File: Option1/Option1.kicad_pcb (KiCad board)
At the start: 2 copper layers, 86 x 62 mm, 122 parts, among them J1 Conn_02x07_Odd_Even, J1301 Conn_01x02_Socket, J1501 GH-13AB, J1801 Conn_01x08_Socket, J401 Conn_01x05_Pin, J402 Conn_01x04_Pin, J403 Conn_01x05_Pin, J503 KF2EDGKRG-3.5-2*7P, J701 Conn_01x02_Socket, Q1001 JY2302, Q1101 JY2302, Q1401 BC817-40, Q1402 BC817-40, Q601 JY2302, Q901 JY2302, SW401 4*4*1.7, U1401 CH340X, U1601 W25Q512JVEIQ, U1701 TJA1051T-3, U1_I/O_Old1 1989780, U201 U7812-500, U202 K7805-500R2_C909663, U203 SY8089AAAC, U204 SY8089AAAC, U2_CAN1 1989780, U301 TJA1051T-3, U302 MCP2515-I/ST, U801 ESP32-WROOM-32E-N4, U802 MCP23017_SO, X301 XL1EL89CSI-111YLC-8M

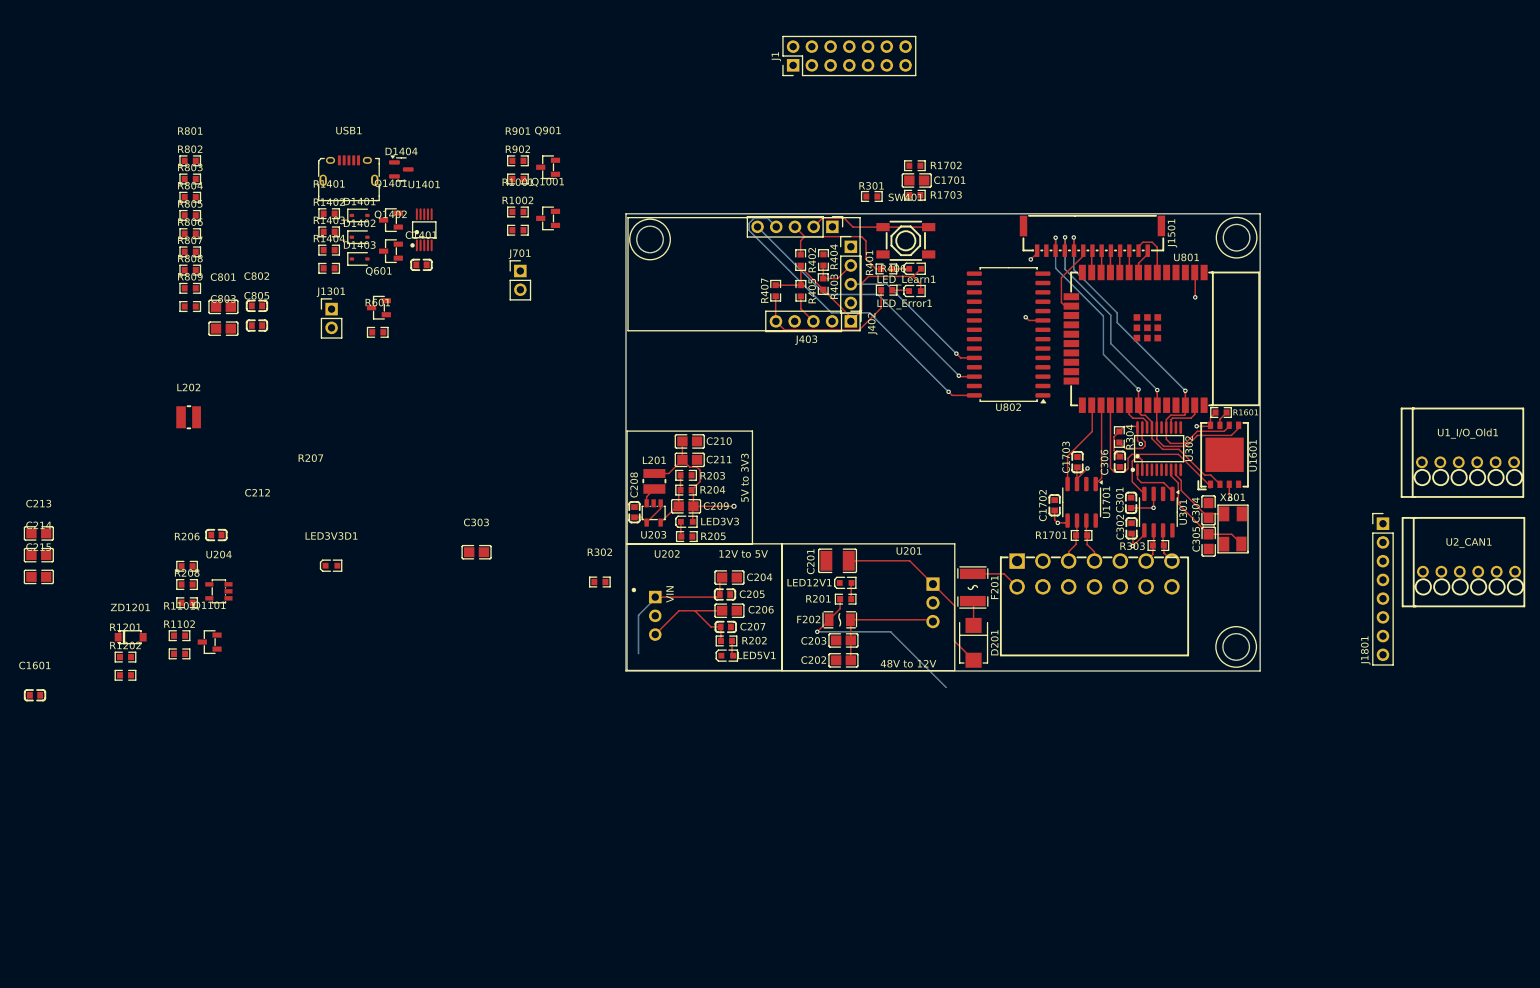
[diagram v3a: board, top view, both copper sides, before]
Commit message: Layout komplett bis auf RFID Leiste und 3V3 Erzeugung Display
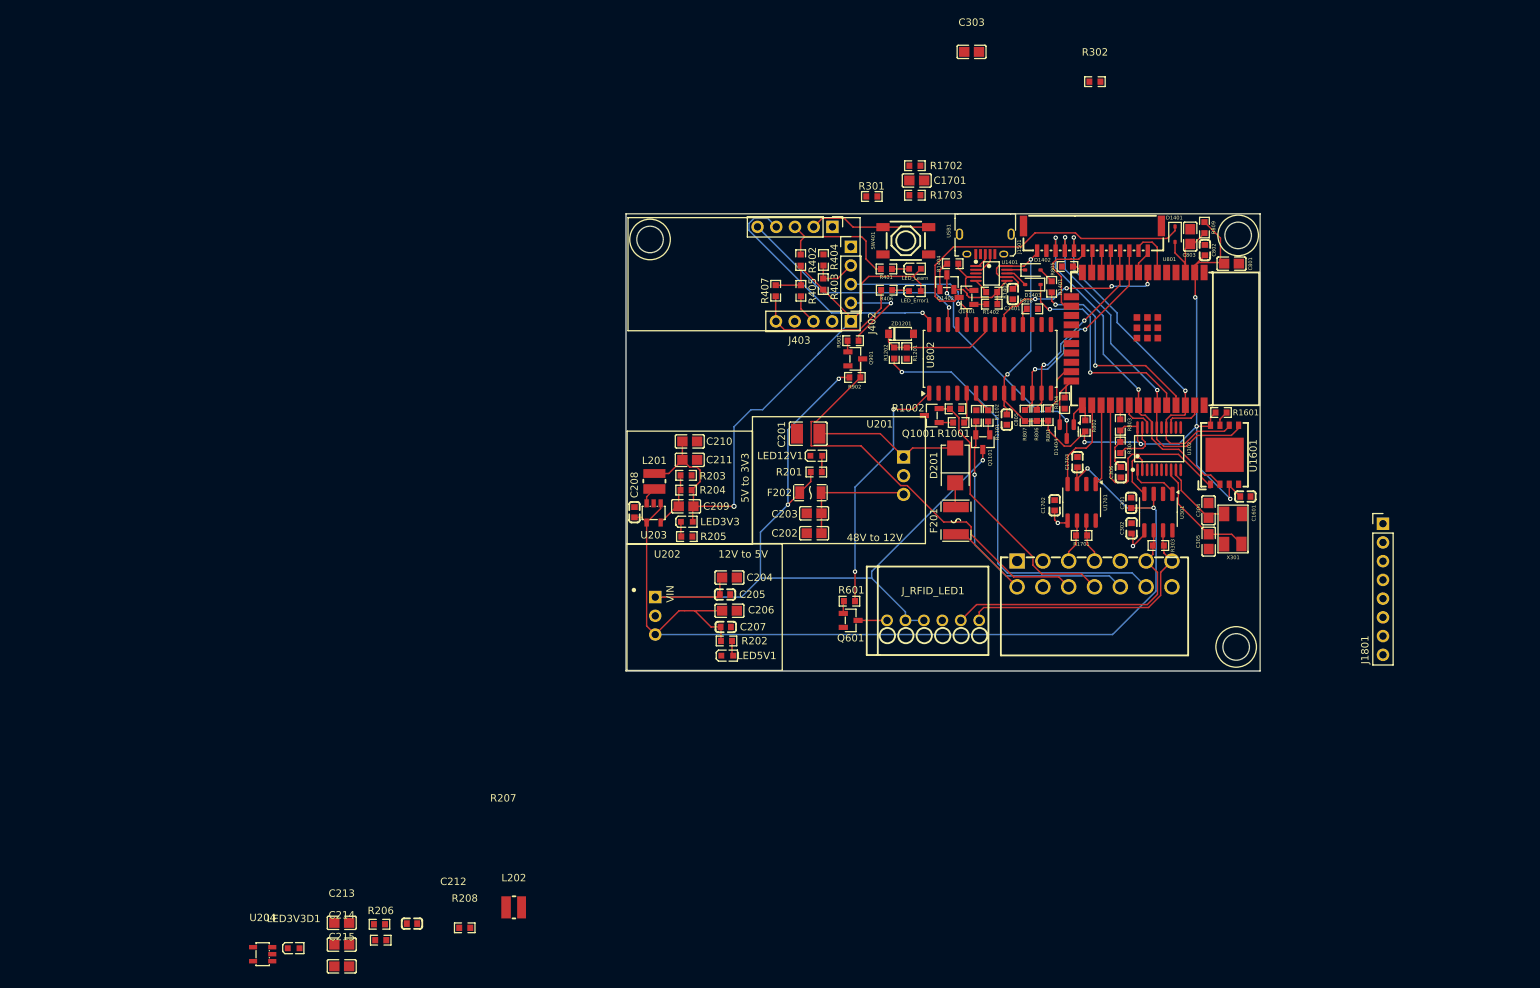
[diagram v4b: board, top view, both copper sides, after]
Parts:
- removed J1: Conn_02x07_Odd_Even, Connector_PinHeader_2.54mm:PinHeader_2x07_P2.54mm_Vertical
- removed J1301, J701: Conn_01x02_Socket, Connector_PinHeader_2.54mm:PinHeader_1x02_P2.54mm_Vertical
- removed U1_I/O_Old1, U2_CAN1: 1989780, easyeda2kicad:CONN-TH_6P-P2.50_1989780
- added J_RFID_LED1: 1989780, easyeda2kicad:CONN-TH_6P-P2.50_1989780, F.Cu at (141.6, 105.1)
- moved C1601 166.3 mm to (183.9, 88.3), turned to 180 degrees
- moved R809 138.0 mm to (178.4, 51.8), turned to -90 degrees
- moved C801 136.8 mm to (182.1, 56.7)
- moved C803 131.7 mm to (176.5, 53.1), turned to -90 degrees
- moved R803 129.9 mm to (167.0, 78.6), turned to 90 degrees
- moved C802 128.8 mm to (178.4, 54.9), turned to 90 degrees
- moved R802 125.9 mm to (162.2, 78.7), turned to 90 degrees
- moved R801 121.4 mm to (157.2, 77.3), turned to 90 degrees
- moved R804 121.3 mm to (159.4, 75.7), turned to -90 degrees
- moved R805 119.0 mm to (159.8, 57.1), turned to 180 degrees
- moved R806 116.9 mm to (155.7, 77.3), turned to -90 degrees
- moved R807 114.9 mm to (154.1, 77.3), turned to -90 degrees
- moved R1202 114.6 mm to (138.0, 68.9), turned to 90 degrees
- moved R808 114.2 mm to (155.1, 62.9)
- moved R1101 113.6 mm to (149.1, 77.4), turned to 90 degrees
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- renumbered LED_Learn1 to LED_Learn
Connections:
- Q601 pad 3: /Stecker LED/Status_LED - -> /Stecker LED - RFID/Status_LED -
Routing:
- net 3.3V: track 86.8 -> 233.1 mm, vias 9 -> 10
- net 5V: track 32.0 -> 140.7 mm
- net 12V: track 45.9 -> 114.2 mm, vias 1 -> 3
- net /Stecker Input/VCU_LED: track 0.00 -> 59.0 mm, vias 0 -> 1
- net /Notaus Schalter/Notaus_VCU: track 0.00 -> 58.6 mm
- net Net-(D1401-K): track 0.00 -> 43.6 mm
- net /SOC Schalter/SOC_VCU: track 0.00 -> 38.9 mm, vias 0 -> 1
- net /RemoteDrive Schalter/RemoteDrive_VCU: track 0.00 -> 36.9 mm
- net /MCT  Wlan/LED_On: track 0.00 -> 33.9 mm, vias 0 -> 2
- net /CAN2_Tranciever/CAN_L: track 4.74 -> 38.0 mm
- net /CAN2_Tranciever/CAN_H: track 4.82 -> 36.8 mm
- net RXD0: track 0.00 -> 30.6 mm, vias 0 -> 2
- net Net-(D1404-Pad3): track 0.00 -> 30.5 mm, vias 0 -> 2
- net TXD0: track 0.00 -> 28.5 mm, vias 0 -> 2
- net IO33: track 2.97 -> 28.9 mm, vias 0 -> 2
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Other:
- outline, holes or cut-outs redrawn

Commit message: 3V3 für Display hinzugefügt und gelayoutet, Brücke zwischen Display und Std 3V3 hinzugefügt in Schaltplan und Platine
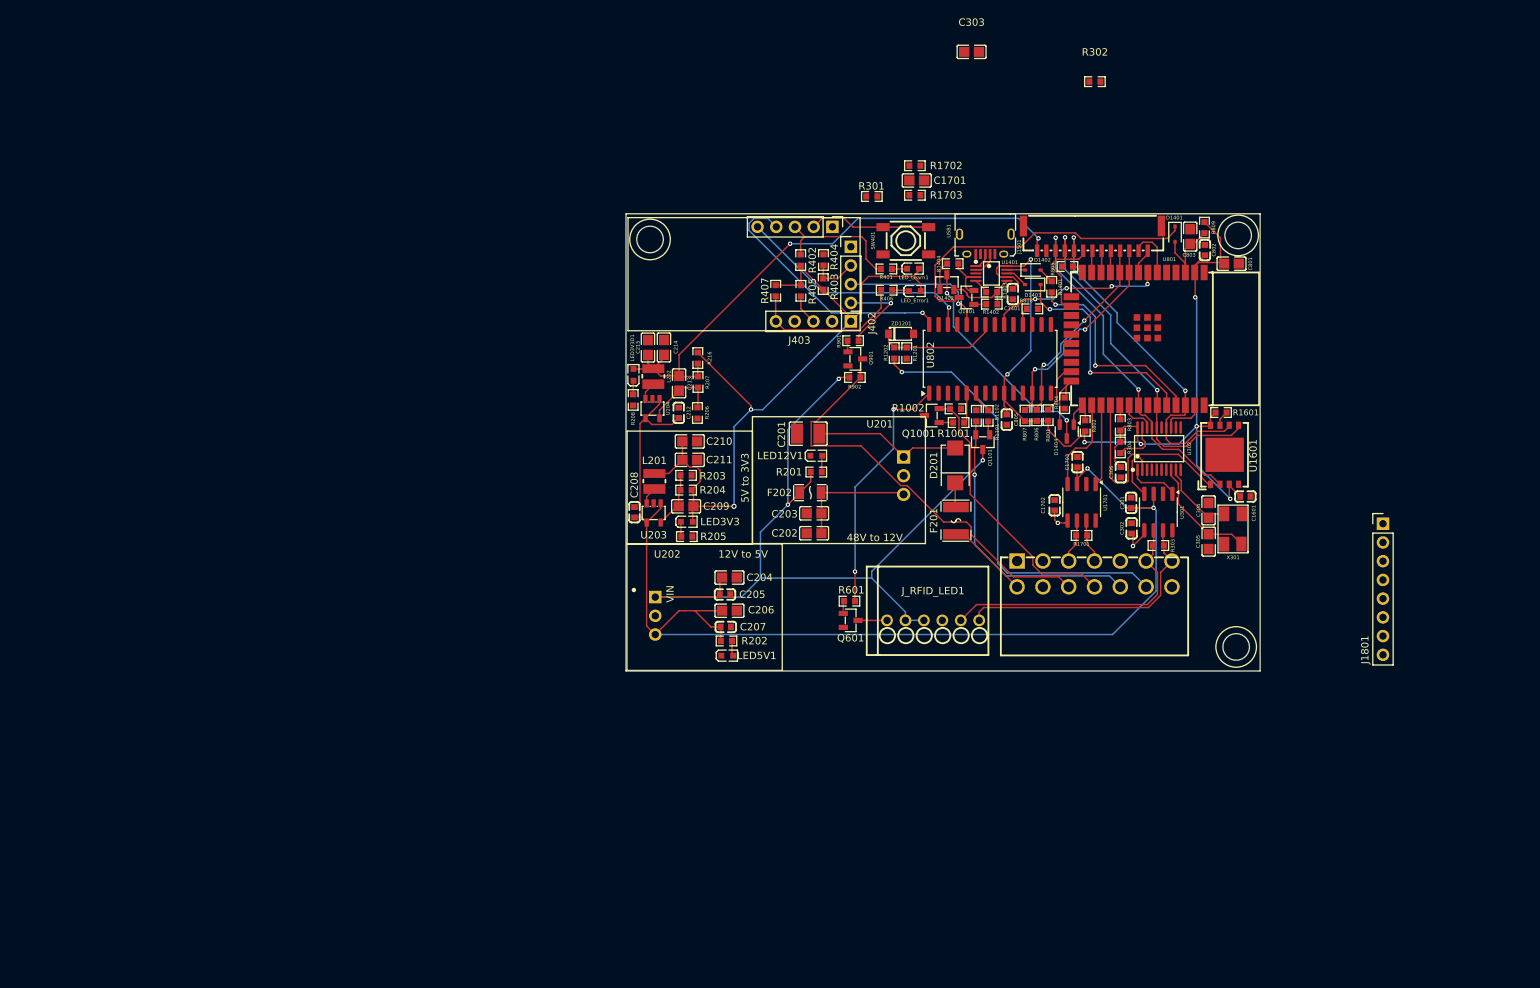
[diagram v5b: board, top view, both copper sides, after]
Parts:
- removed LED_Learn: XL-1608SYGC-06, easyeda2kicad:LED0603-RD_GREEN
- added LED_Learn1: XL-1608SYGC-06, easyeda2kicad:LED0603-RD_GREEN, F.Cu at (138.9, 57.4)
- added R216: 0Ω, easyeda2kicad:R0603, F.Cu at (109.7, 69.5)
- moved C215 93.6 mm to (102.9, 68.1), turned to 90 degrees
- moved C214 92.0 mm to (105.1, 68.1), turned to 90 degrees
- moved U204 90.9 mm to (103.5, 76.4), turned to 90 degrees
- moved LED3V3D1 90.4 mm to (101.0, 71.8), turned to 90 degrees
- moved C213 86.3 mm to (107.1, 73.0), turned to -90 degrees
- moved R207 85.3 mm to (109.7, 72.8), turned to -90 degrees
- moved R206 83.4 mm to (109.6, 77.0), turned to -90 degrees
- moved C212 78.1 mm to (107.1, 77.0), turned to 90 degrees
- moved R208 75.1 mm to (100.9, 75.2), turned to -90 degrees
- moved L202 74.4 mm to (103.7, 72.0), turned to 90 degrees
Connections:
- C213 pad 1: 3.3V -> /Powersupply/3.3V_D
- C214 pad 1: 3.3V -> /Powersupply/3.3V_D
- C215 pad 1: 3.3V -> /Powersupply/3.3V_D
- J1501 pad 13: 3.3V -> /Powersupply/3.3V_D
- L202 pad 2: 3.3V -> /Powersupply/3.3V_D
- LED3V3D1 pad 2: 3.3V -> /Powersupply/3.3V_D
- R207 pad 1: 3.3V -> /Powersupply/3.3V_D
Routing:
- net /Powersupply/3.3V_D: track 0.00 -> 77.8 mm, vias 0 -> 2
- net 5V: track 140.7 -> 164.1 mm
- net Net-(U204-FB): track 0.00 -> 10.3 mm
- net 3.3V: track 233.1 -> 242.3 mm, vias 10 -> 11
- net Net-(U204-LX): track 0.00 -> 2.46 mm
- net Net-(LED3V3D1-K): track 0.00 -> 1.87 mm

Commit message: GND polygon hinzugefügt, unverbundene Pads verknüpft, 0 Ohm Widerstand für Display Strohmversorgung hinzugefügt
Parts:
- removed C1701, C303: 4.7nF, easyeda2kicad:C0805
- removed R1702, R1703, R301, R302: 33k, easyeda2kicad:R0603
- added R217: 0Ω, easyeda2kicad:R0603, F.Cu at (113.5, 72.7)
- moved J1801 62.7 mm to (163.4, 43.1), turned to -90 degrees
- moved C215 9.74 mm to (111.4, 73.0), turned to -90 degrees
- moved C214 6.41 mm to (109.3, 73.0), turned to -90 degrees
- moved R216 6.37 mm to (115.2, 72.7), turned to -90 degrees
- moved R207 3.20 mm to (109.8, 76.0), turned to 180 degrees
- moved R206 0.79 mm to (109.8, 77.8), turned to 180 degrees
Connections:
- C213 pad 1: /Powersupply/3.3V_D -> /Powersupply/3.3V_D1
- C214 pad 1: /Powersupply/3.3V_D -> /Powersupply/3.3V_D1
- C215 pad 1: /Powersupply/3.3V_D -> /Powersupply/3.3V_D1
- L202 pad 2: /Powersupply/3.3V_D -> /Powersupply/3.3V_D1
- LED3V3D1 pad 2: /Powersupply/3.3V_D -> /Powersupply/3.3V_D1
- R207 pad 1: /Powersupply/3.3V_D -> /Powersupply/3.3V_D1
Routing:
- net 3.3V: track 242.3 -> 307.0 mm, vias 11 -> 10
- net /CAN2_Tranciever/CAN_S-Mode: track 0.00 -> 55.4 mm, vias 0 -> 2
- net LED_Modus: track 18.1 -> 60.6 mm, vias 0 -> 2
- net /CAN1 Tranciever/CAN_S-Mode: track 0.00 -> 33.4 mm, vias 0 -> 2
- net /Powersupply/3.3V_D1: track 0.00 -> 19.2 mm
- net Fehler_LED: track 21.8 -> 38.5 mm
- net /Powersupply/3.3V_D: track 77.8 -> 62.8 mm
- net 12V: track 114.2 -> 127.9 mm, vias 3 -> 4
- net 5V: track 164.1 -> 174.3 mm
- net /SOC Schalter/SOC_VCU: track 38.9 -> 41.9 mm
- net Net-(U204-FB): track 10.3 -> 7.66 mm
- added copper zone on B.Cu, net GND
- added copper zone on F.Cu, net GND
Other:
- outline, holes or cut-outs redrawn
